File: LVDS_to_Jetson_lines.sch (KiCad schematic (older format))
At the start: 22 parts, among them IC1 SN74AVC4T245PWR, U5 TS3DDR3812_RUA_42, U6 TS3DDR3812_RUA_42, U8 SN74AVCH16T245_DGV_48

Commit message: added enable line for slow signals
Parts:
- added R27, R28: 0, Resistors_SMD:R_0805, symbol Device:R
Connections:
- net CSI_C_CLK_N: now also U5.13 (A8); no longer U6.6 (A4)
- net CSI_C_CLK_P: now also U5.14 (A9); no longer U6.7 (A5)
- net CSI_D_D0_N: now also U6.6 (A4); no longer U5.13 (A8)
- net CSI_D_D0_P: now also U6.7 (A5); no longer U5.14 (A9)
- net CSI_D_D1_N: now also U6.4 (A2); no longer U5.11 (A6)
- net CSI_D_D1_P: now also U6.5 (A3); no longer U5.12 (A7)
- net HS_CSI_C_CLK_N: now also U5.25 (B8); no longer U6.34 (B4)
- net HS_CSI_C_CLK_P: now also U5.23 (B9); no longer U6.32 (B5)
- net HS_CSI_D_D0_N: now also U6.34 (B4); no longer U5.25 (B8)
- net HS_CSI_D_D0_P: now also U6.32 (B5); no longer U5.23 (B9)
- net HS_CSI_D_D1_N: now also U6.38 (B2); no longer U5.29 (B6)
- net HS_CSI_D_D1_P: now also U6.36 (B3); no longer U5.27 (B7)
- net LP_CSI_C_CLK_N: now also U5.24 (C8); no longer U6.33 (C4)
- net LP_CSI_C_CLK_P: now also U5.22 (C9); no longer U6.31 (C5)
- net LP_CSI_D_D0_N: now also U6.33 (C4); no longer U5.24 (C8)
- net LP_CSI_D_D0_P: now also U6.31 (C5); no longer U5.22 (C9)
- net LP_CSI_D_D1_N: now also U6.37 (C2); no longer U5.28 (C6)
- net LP_CSI_D_D1_P: now also U6.35 (C3); no longer U5.26 (C7)
- net EN_MIPI_OUT_CLOCK_3V3 renamed EN_MIPI_OUT_CSI_D
- net EN_MIPI_OUT_DATA_3V3 renamed EN_MIPI_OUT_CSI_C
- net SWITCH_CLOCK_LANES_3V3 renamed SWITCH_CLOCK_LANES_CSI_CD
- net SWITCH_CLOCK_LANES_CSI_CD: now also R27.2, R28.2; no longer R1.2
- net SWITCH_DATA_LANES_3V3 renamed SWITCH_DATA_LANES_CSI_CD
- net SWITCH_DATA_LANES_CSI_CD: now also R1.2
- net SWITCH_U5 renamed SWITCH1_U5
- net SWITCH1_U5: no longer U5.10 (SEL2)
- net SWITCH_U6 renamed SWITCH1_U6
- net SWITCH1_U6: no longer U6.10 (SEL2)
- new net SWITCH2_U5: R27.1, U5.10 (SEL2)
- new net SWITCH2_U6: R28.1, U6.10 (SEL2)
- no-connect marks 35 -> 30
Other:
- note added: "Note: HS and clock lanes has a separate switch pins\n1) Enable shorter LP state for clock lanes, as required in D-PHY standard\n2) Enable continious mode for clock"
- note added: "Switches U5 and U6, A to B level shift from VADJ to 3p3 volt"
- note removed: "Note: HS and clock lanes has a separate switch IC's, this is for tow reasons:\n1) Enable shorter LP state for clock lanes, as required in D-PHY standard\n2) Enable continious mode for clock"
- note removed: "Switches U5 and U6, SEL1,2 level shift from VADJ to 3p3 volt"

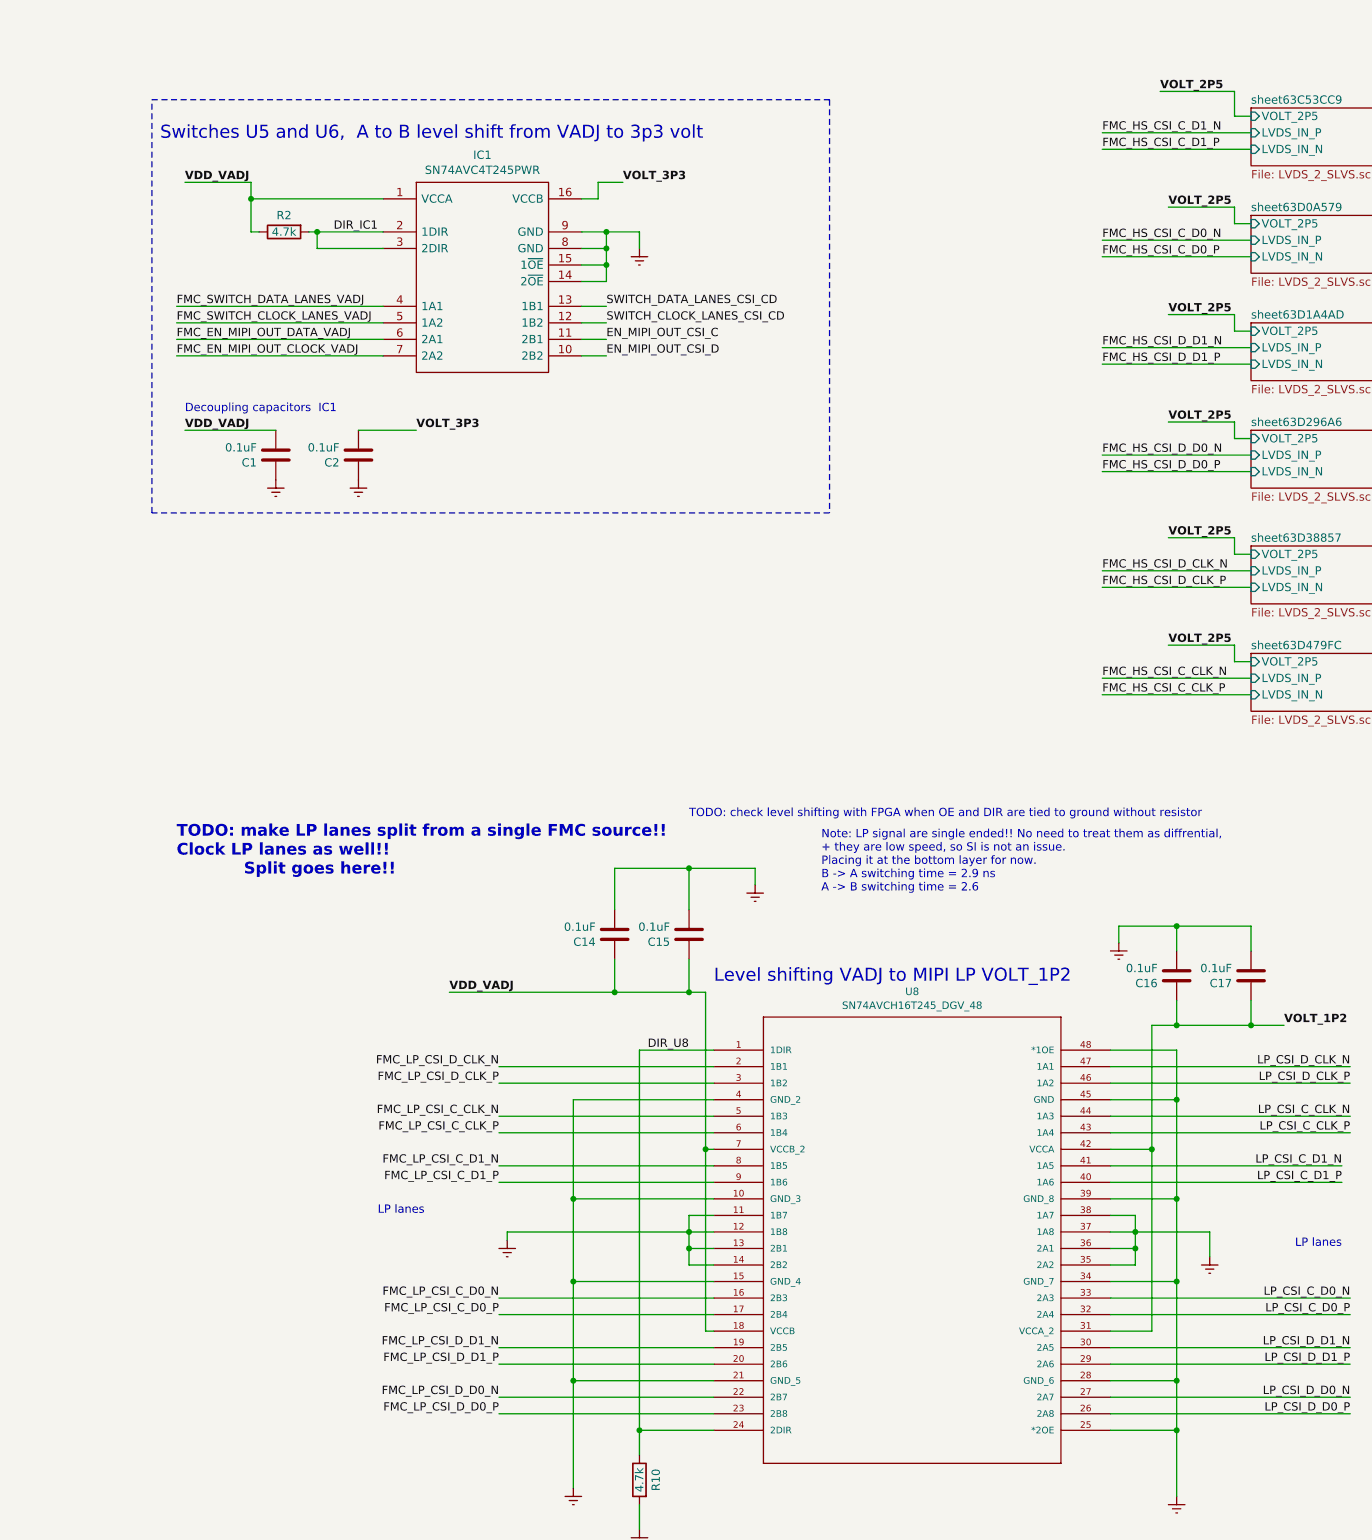
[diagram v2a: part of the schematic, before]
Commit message: Added dummy nets to FMC connector
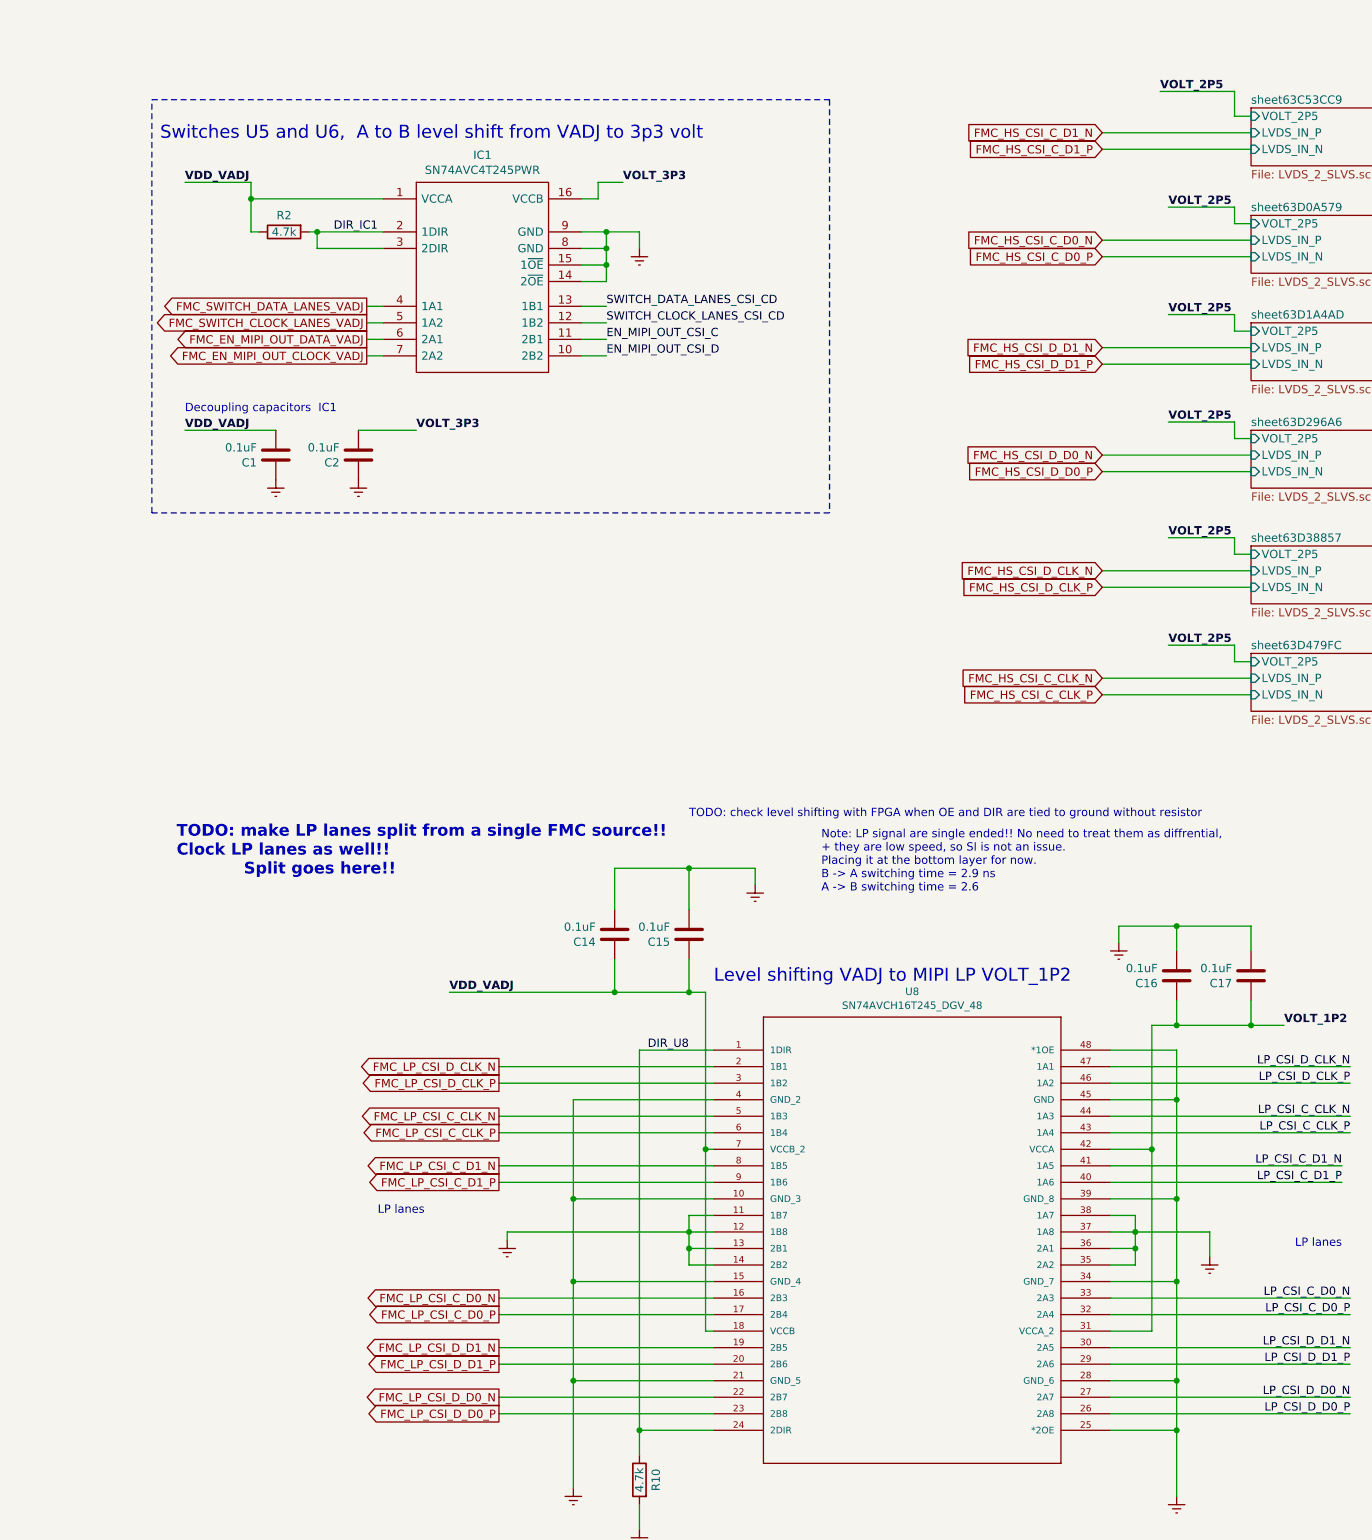
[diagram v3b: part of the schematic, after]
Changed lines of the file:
@@
 Text Label 8900 2150 0    50   ~ 0
 HS_CSI_C_D1_P
-Text Label 6400 2050 0    50   ~ 0
-FMC_HS_CSI_C_D1_N
-Text Label 6400 2150 0    50   ~ 0
-FMC_HS_CSI_C_D1_P
 $Sheet
 S 7300 2550 1250 350
@@
 Text Label 6800 5150 0    50   ~ 10
 VOLT_2P5
-Text Label 6400 2700 0    50   ~ 0
-FMC_HS_CSI_C_D0_N
-Text Label 6400 2800 0    50   ~ 0
-FMC_HS_CSI_C_D0_P
-Text Label 6400 3350 0    50   ~ 0
-FMC_HS_CSI_D_D1_N
-Text Label 6400 3450 0    50   ~ 0
-FMC_HS_CSI_D_D1_P
-Text Label 6400 4000 0    50   ~ 0
-FMC_HS_CSI_D_D0_N
-Text Label 6400 4100 0    50   ~ 0
-FMC_HS_CSI_D_D0_P
-Text Label 6400 4800 0    50   ~ 0
-FMC_HS_CSI_D_CLK_P
-Text Label 6400 5350 0    50   ~ 0
-FMC_HS_CSI_C_CLK_N
-Text Label 6400 5450 0    50   ~ 0
-FMC_HS_CSI_C_CLK_P
 Wire Wire Line
 	6400 2700 7300 2700
@@
 Wire Wire Line
 	7300 5450 6400 5450
-Text Label 6400 4700 0    50   ~ 0
-FMC_HS_CSI_D_CLK_N
-Text Label 2750 8400 2    50   ~ 0
-FMC_LP_CSI_C_D1_P
-Text Label 2750 8300 2    50   ~ 0
-FMC_LP_CSI_C_D1_N
-Text Label 2750 9100 2    50   ~ 0
-FMC_LP_CSI_C_D0_N
-Text Label 2750 9200 2    50   ~ 0
-FMC_LP_CSI_C_D0_P
-Text Label 2750 9400 2    50   ~ 0
-FMC_LP_CSI_D_D1_N
-Text Label 2750 9500 2    50   ~ 0
-FMC_LP_CSI_D_D1_P
-Text Label 2750 9800 2    50   ~ 0
-FMC_LP_CSI_D_D0_P
-Text Label 2750 9700 2    50   ~ 0
-FMC_LP_CSI_D_D0_N
 Text Notes 2300 8600 2    50   ~ 0
 LP lanes
@@
 	3250 3100 3400 3100
 Wire Wire Line
-	2050 3100 800  3100
-Text Label 800  3100 0    50   ~ 0
-FMC_SWITCH_DATA_LANES_VADJ
+	2050 3100 1950 3100
 Text Notes 700  2100 0    79   ~ 0
 Switches U5 and U6,  A to B level shift from VADJ to 3p3 volt
@@
 	3250 3200 3400 3200
 Wire Wire Line
-	2050 3200 800  3200
-Text Label 800  3200 0    50   ~ 0
-FMC_SWITCH_CLOCK_LANES_VADJ
+	2050 3200 1950 3200
 Wire Wire Line
 	15450 7800 15550 7800
@@
 Text Label 14650 7800 0    50   ~ 0
 SWITCH1_U6
-Text Label 2750 8100 2    50   ~ 0
-FMC_LP_CSI_C_CLK_P
-Text Label 2750 8000 2    50   ~ 0
-FMC_LP_CSI_C_CLK_N
 Wire Wire Line
 	4050 8100 2750 8100
@@
 Wire Wire Line
 	2750 7700 4050 7700
-Text Label 2750 7800 2    50   ~ 0
-FMC_LP_CSI_D_CLK_P
-Text Label 2750 7700 2    50   ~ 0
-FMC_LP_CSI_D_CLK_N
 Text Notes 800  6550 0    71   ~ 14
 TODO: make LP lanes split from a single FMC source!!\nClock LP lanes as well!!\n            Split goes here!!
@@
 Wire Wire Line
 	3250 3300 3400 3300
-Text Label 800  3300 0    50   ~ 0
-FMC_EN_MIPI_OUT_DATA_VADJ
-Text Label 800  3400 0    50   ~ 0
-FMC_EN_MIPI_OUT_CLOCK_VADJ
-Wire Wire Line
-	800  3300 2050 3300
-Wire Wire Line
-	800  3400 2050 3400
+Wire Wire Line
+	1950 3300 2050 3300
+Wire Wire Line
+	1950 3400 2050 3400
 Text GLabel 14750 6700 2    50   Output ~ 0
 CSI_D_D0_P
@@
 	-1   0    0    1
 $EndComp
+Text GLabel 1950 3100 0    50   Output ~ 0
+FMC_SWITCH_DATA_LANES_VADJ
+Text GLabel 1950 3400 0    50   Output ~ 0
+FMC_EN_MIPI_OUT_CLOCK_VADJ
+Text GLabel 1950 3300 0    50   Output ~ 0
+FMC_EN_MIPI_OUT_DATA_VADJ
+Text GLabel 1950 3200 0    50   Output ~ 0
+FMC_SWITCH_CLOCK_LANES_VADJ
+Text GLabel 2750 7800 0    50   Output ~ 0
+FMC_LP_CSI_D_CLK_P
+Text GLabel 2750 8000 0    50   Output ~ 0
+FMC_LP_CSI_C_CLK_N
+Text GLabel 2750 8100 0    50   Output ~ 0
+FMC_LP_CSI_C_CLK_P
+Text GLabel 2750 8300 0    50   Output ~ 0
+FMC_LP_CSI_C_D1_N
+Text GLabel 2750 8400 0    50   Output ~ 0
+FMC_LP_CSI_C_D1_P
+Text GLabel 2750 9100 0    50   Output ~ 0
+FMC_LP_CSI_C_D0_N
+Text GLabel 2750 9200 0    50   Output ~ 0
+FMC_LP_CSI_C_D0_P
+Text GLabel 2750 9400 0    50   Output ~ 0
+FMC_LP_CSI_D_D1_N
+Text GLabel 2750 9500 0    50   Output ~ 0
+FMC_LP_CSI_D_D1_P
+Text GLabel 2750 9800 0    50   Output ~ 0
+FMC_LP_CSI_D_D0_P
+Text GLabel 2750 7700 0    50   Output ~ 0
+FMC_LP_CSI_D_CLK_N
+Text GLabel 2750 9700 0    50   Output ~ 0
+FMC_LP_CSI_D_D0_N
+Text GLabel 6400 2050 0    50   Input ~ 0
+FMC_HS_CSI_C_D1_N
+Text GLabel 6400 2150 0    50   Input ~ 0
+FMC_HS_CSI_C_D1_P
+Text GLabel 6400 2700 0    50   Input ~ 0
+FMC_HS_CSI_C_D0_N
+Text GLabel 6400 2800 0    50   Input ~ 0
+FMC_HS_CSI_C_D0_P
+Text GLabel 6400 3350 0    50   Input ~ 0
+FMC_HS_CSI_D_D1_N
+Text GLabel 6400 3450 0    50   Input ~ 0
+FMC_HS_CSI_D_D1_P
+Text GLabel 6400 4000 0    50   Input ~ 0
+FMC_HS_CSI_D_D0_N
+Text GLabel 6400 4100 0    50   Input ~ 0
+FMC_HS_CSI_D_D0_P
+Text GLabel 6400 4700 0    50   Input ~ 0
+FMC_HS_CSI_D_CLK_N
+Text GLabel 6400 4800 0    50   Input ~ 0
+FMC_HS_CSI_D_CLK_P
+Text GLabel 6400 5350 0    50   Input ~ 0
+FMC_HS_CSI_C_CLK_N
+Text GLabel 6400 5450 0    50   Input ~ 0
+FMC_HS_CSI_C_CLK_P
 $EndSCHEMATC
